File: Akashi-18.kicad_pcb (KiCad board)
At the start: 2 copper layers, 71.1 x 83.8 mm, 12 parts, among them Q1 DTC143Z, Q2 DTC143Z, Q3 DTC143Z, SW1 B3FS, SW2 B3FS, SW3 B3FS, U1 Pico

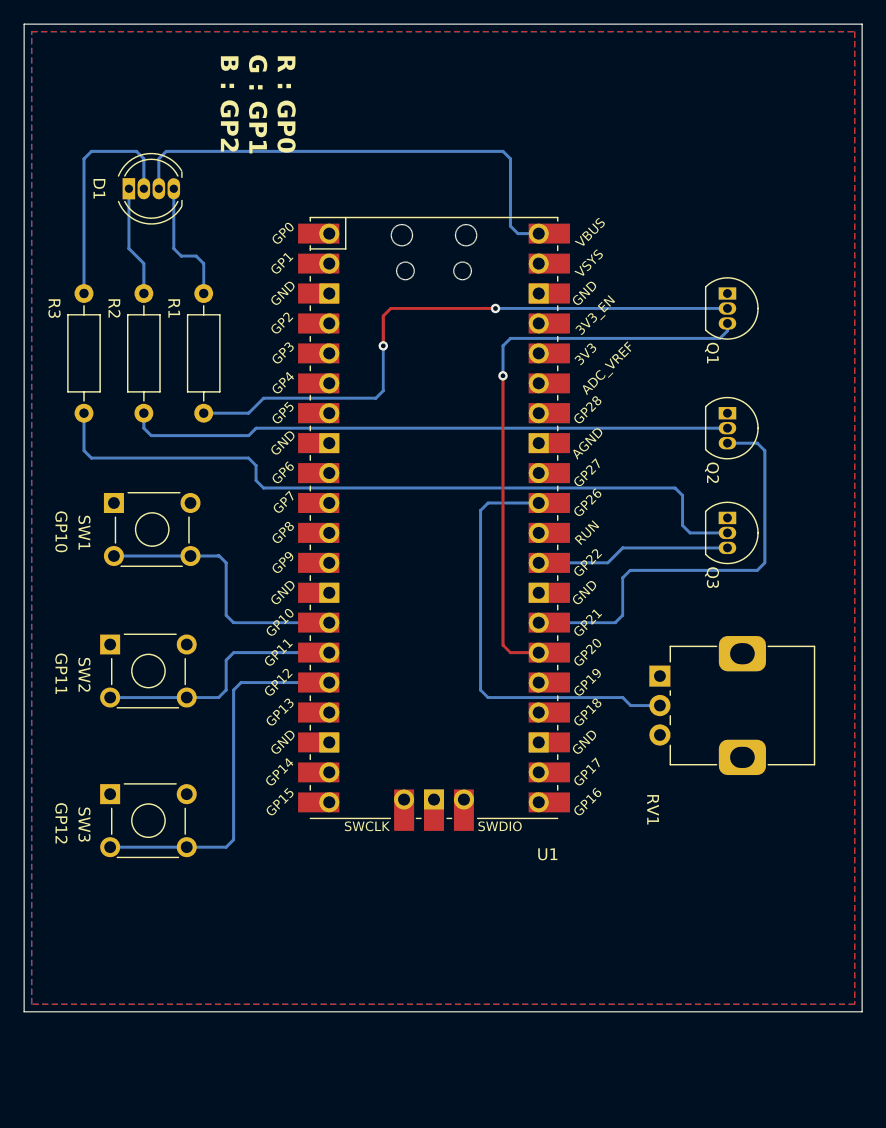
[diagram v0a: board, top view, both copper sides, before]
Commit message: All modified parts are registered to the local lib.
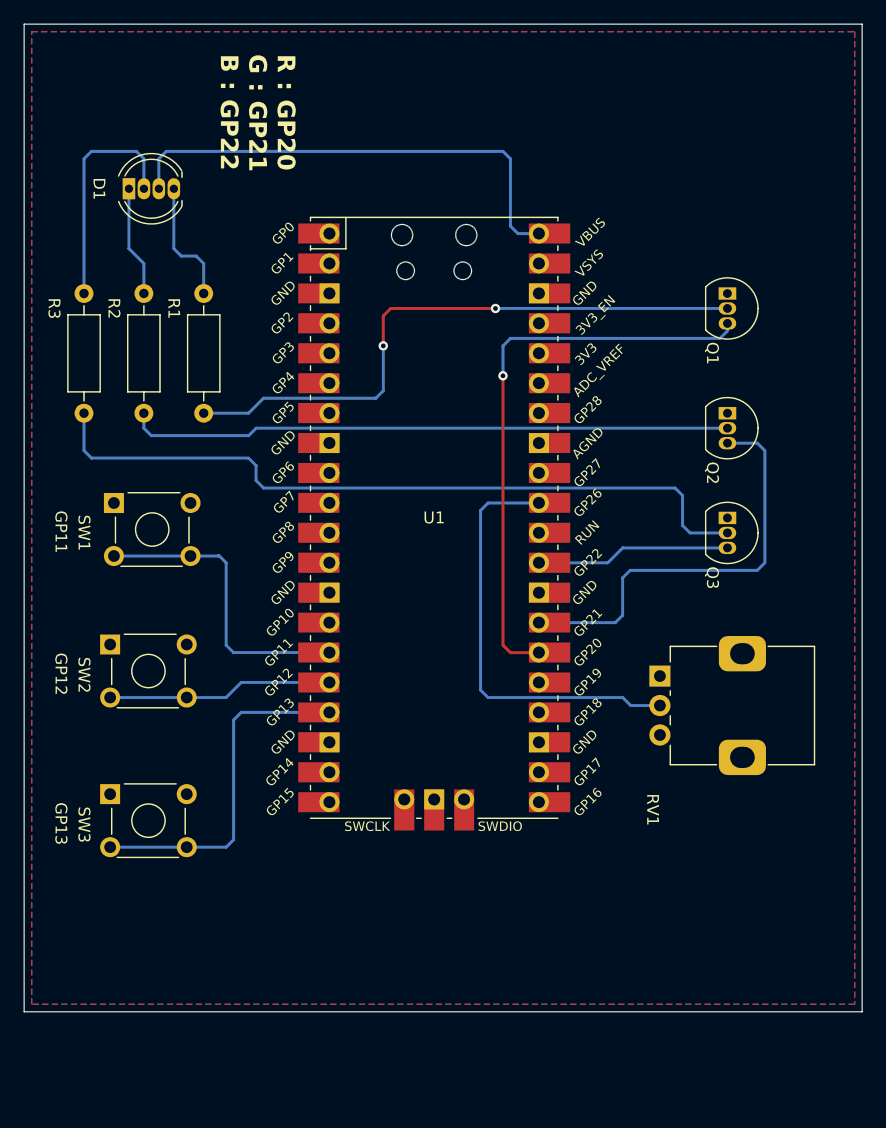
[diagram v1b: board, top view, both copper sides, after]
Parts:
- D1: footprint LED_THT:LED_D5.0mm-4_RGB -> My_Lib:LED_D5.0mm-4_RGB
- U1: footprint Rpi_Pico:RPi_Pico_SMD_TH -> My_Lib:RPi_Pico_SMD_TH
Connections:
- SW1 pad 2: Net-(U1-GPIO10) -> Net-(U1-GPIO11)
- SW2 pad 2: Net-(U1-GPIO11) -> Net-(U1-GPIO12)
- SW3 pad 2: Net-(U1-GPIO12) -> Net-(U1-GPIO13)
- U1 pad 14: Net-(U1-GPIO10) -> unconnected-(U1-GPIO10-Pad14)
- U1 pad 17: unconnected-(U1-GPIO13-Pad17) -> Net-(U1-GPIO13)
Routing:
- net Net-(U1-GPIO13): track 0.00 -> 29.3 mm
- net Net-(U1-GPIO10): track 23.3 -> 0.00 mm
- net Net-(U1-GPIO12): track 31.8 -> 19.1 mm
- net Net-(U1-GPIO11): track 21.7 -> 25.8 mm
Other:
- board text added: "GP13"
- board text added: "Pico Trainer"
- board text added: "R : GP20 G : GP21 B : GP22"
- board text removed: "GP10"
- board text removed: "R : GP0 G : GP1 B : GP2"

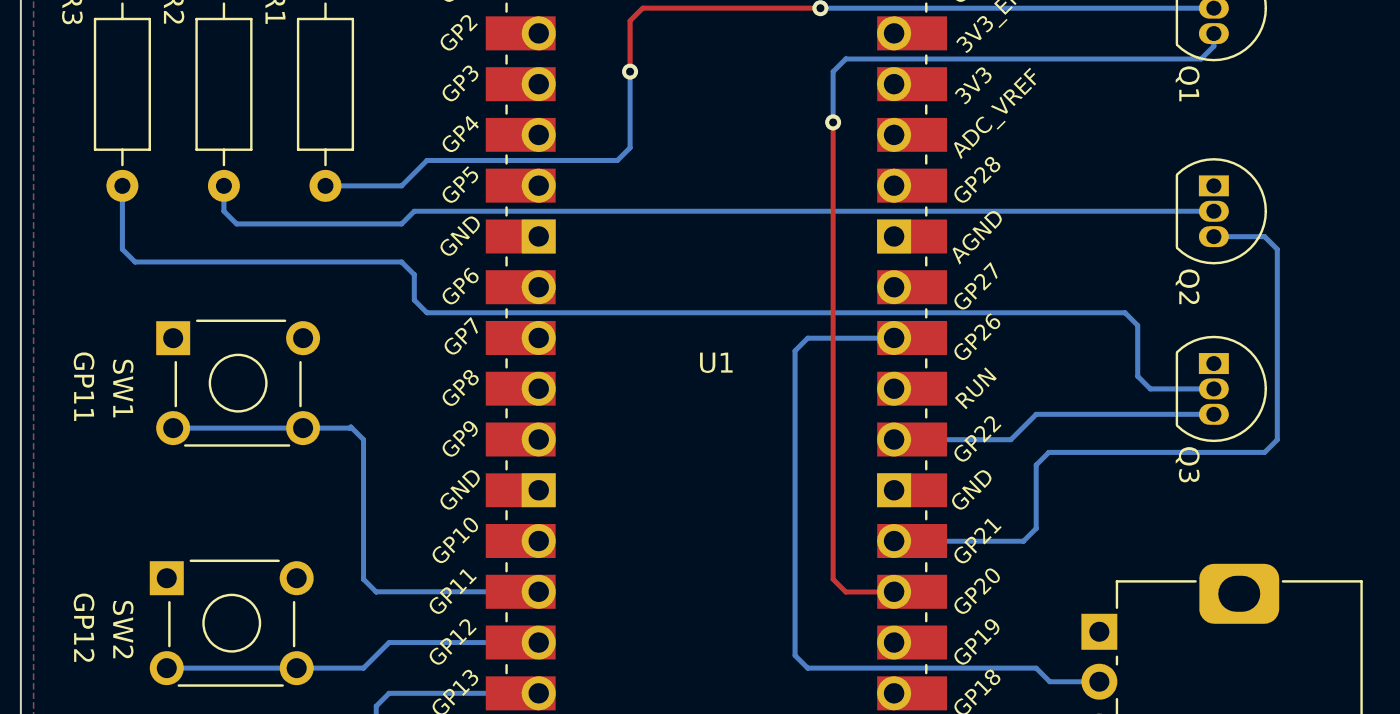
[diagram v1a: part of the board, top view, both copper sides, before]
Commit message: Adjust the space of transistor.
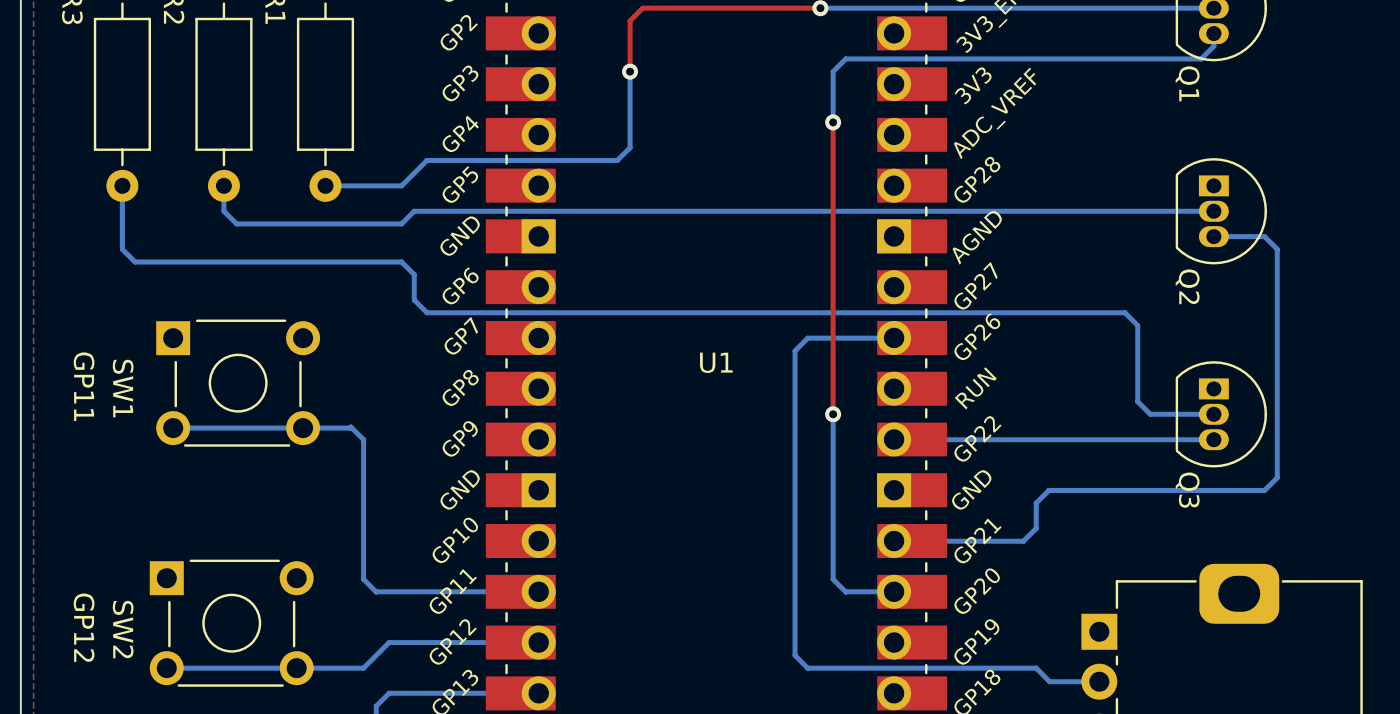
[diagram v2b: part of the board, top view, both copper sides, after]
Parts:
- R1: value R -> 220
- R2: value R -> 180
- R3: value R -> 91
- moved Q3 1.27 mm to (148.6, 94.0)
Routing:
- net Net-(Q3-C): track 62.9 -> 64.2 mm
- net /BLUE: track 16.5 -> 16.0 mm
- net /RED: vias 1 -> 2
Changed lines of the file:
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@@
         (effects (font (size 1 1) (thickness 0.15)))
     )
-    (fp_text value "R" (at 5.08 2.37 90) (layer "F.Fab")
+    (fp_text value "220" (at 5.08 2.37 90) (layer "F.Fab")
         (effects (font (size 1 1) (thickness 0.15)))
     )
@@
         (effects (font (size 1 1) (thickness 0.15)))
     )
-    (fp_text value "R" (at 5.08 2.37 90) (layer "F.Fab")
+    (fp_text value "91" (at 5.08 2.37 90) (layer "F.Fab")
         (effects (font (size 1 1) (thickness 0.15)))
     )
@@
         (effects (font (size 1 1) (thickness 0.15)))
     )
-    (fp_text value "R" (at 5.08 2.37 90) (layer "F.Fab")
+    (fp_text value "180" (at 5.08 2.37 90) (layer "F.Fab")
         (effects (font (size 1 1) (thickness 0.15)))
     )
@@
   )
   (footprint "Package_TO_SOT_THT:TO-92_Inline" (layer "F.Cu")
-    (at 148.59 92.71 -90)
+    (at 148.59 93.98 -90)
     (descr "TO-92 leads in-line, narrow, oval pads, drill 0.75mm (see NXP sot054_po.pdf)")
     (tags "to-92 sc-43 sc-43a sot54 PA33 transistor")
@@
   (segment (start 109.22 82.55) (end 107.95 83.82) (width 0.25) (layer "B.Cu") (net 6))
   (segment (start 119.38 81.915) (end 118.745 82.55) (width 0.25) (layer "B.Cu") (net 6))
-  (segment (start 129.54 103.505) (end 130.175 104.14) (width 0.25) (layer "F.Cu") (net 7))
-  (segment (start 129.54 80.645) (end 129.54 103.505) (width 0.25) (layer "F.Cu") (net 7))
-  (segment (start 130.175 104.14) (end 132.575 104.14) (width 0.25) (layer "F.Cu") (net 7))
+  (segment (start 129.54 80.645) (end 129.54 95.25) (width 0.25) (layer "F.Cu") (net 7))
+  (via (at 129.54 95.25) (size 0.8) (drill 0.4) (layers "F.Cu" "B.Cu") (net 7))
   (via (at 129.54 80.645) (size 0.8) (drill 0.4) (layers "F.Cu" "B.Cu") (net 7))
   (segment (start 147.955 77.47) (end 130.175 77.47) (width 0.25) (layer "B.Cu") (net 7))
+  (segment (start 130.175 104.14) (end 129.54 103.505) (width 0.25) (layer "B.Cu") (net 7))
+  (segment (start 129.54 103.505) (end 129.54 95.25) (width 0.25) (layer "B.Cu") (net 7))
   (segment (start 148.59 76.835) (end 147.955 77.47) (width 0.25) (layer "B.Cu") (net 7))
   (segment (start 129.54 78.105) (end 129.54 80.645) (width 0.25) (layer "B.Cu") (net 7))
+  (segment (start 132.59 104.13) (end 130.185 104.13) (width 0.25) (layer "B.Cu") (net 7))
+  (segment (start 130.185 104.13) (end 130.175 104.14) (width 0.25) (layer "B.Cu") (net 7))
   (segment (start 148.59 76.2) (end 148.59 76.835) (width 0.25) (layer "B.Cu") (net 7))
   (segment (start 130.175 77.47) (end 129.54 78.105) (width 0.25) (layer "B.Cu") (net 7))
@@
   (segment (start 99.695 85.725) (end 99.06 85.09) (width 0.25) (layer "B.Cu") (net 8))
   (segment (start 99.06 85.09) (end 99.06 83.82) (width 0.25) (layer "B.Cu") (net 8))
-  (segment (start 148.59 86.36) (end 151.13 86.36) (width 0.25) (layer "B.Cu") (net 9))
-  (segment (start 151.13 97.155) (end 140.335 97.155) (width 0.25) (layer "B.Cu") (net 9))
-  (segment (start 151.765 96.52) (end 151.13 97.155) (width 0.25) (layer "B.Cu") (net 9))
-  (segment (start 139.7 100.965) (end 139.065 101.6) (width 0.25) (layer "B.Cu") (net 9))
-  (segment (start 139.7 97.79) (end 139.7 100.965) (width 0.25) (layer "B.Cu") (net 9))
-  (segment (start 140.335 97.155) (end 139.7 97.79) (width 0.25) (layer "B.Cu") (net 9))
-  (segment (start 151.13 86.36) (end 151.765 86.995) (width 0.25) (layer "B.Cu") (net 9))
-  (segment (start 151.765 86.995) (end 151.765 96.52) (width 0.25) (layer "B.Cu") (net 9))
-  (segment (start 139.065 101.6) (end 132.575 101.6) (width 0.25) (layer "B.Cu") (net 9))
-  (segment (start 145.415 93.98) (end 144.78 93.345) (width 0.25) (layer "B.Cu") (net 10))
-  (segment (start 94.615 87.63) (end 93.98 86.995) (width 0.25) (layer "B.Cu") (net 10))
-  (segment (start 108.585 89.535) (end 108.585 88.265) (width 0.25) (layer "B.Cu") (net 10))
-  (segment (start 144.78 90.805) (end 144.145 90.17) (width 0.25) (layer "B.Cu") (net 10))
-  (segment (start 144.145 90.17) (end 109.22 90.17) (width 0.25) (layer "B.Cu") (net 10))
-  (segment (start 107.95 87.63) (end 94.615 87.63) (width 0.25) (layer "B.Cu") (net 10))
-  (segment (start 148.59 93.98) (end 145.415 93.98) (width 0.25) (layer "B.Cu") (net 10))
-  (segment (start 108.585 88.265) (end 107.95 87.63) (width 0.25) (layer "B.Cu") (net 10))
-  (segment (start 93.98 86.995) (end 93.98 83.82) (width 0.25) (layer "B.Cu") (net 10))
-  (segment (start 144.78 93.345) (end 144.78 90.805) (width 0.25) (layer "B.Cu") (net 10))
-  (segment (start 109.22 90.17) (end 108.585 89.535) (width 0.25) (layer "B.Cu") (net 10))
-  (segment (start 139.7 95.25) (end 138.43 96.52) (width 0.25) (layer "B.Cu") (net 11))
-  (segment (start 138.43 96.52) (end 132.575 96.52) (width 0.25) (layer "B.Cu") (net 11))
-  (segment (start 148.59 95.25) (end 139.7 95.25) (width 0.25) (layer "B.Cu") (net 11))
+  (segment (start 139.065 101.6) (end 139.7 100.965) (width 0.25) (layer "B.Cu") (net 9))
+  (segment (start 139.7 99.695) (end 140.335 99.06) (width 0.25) (layer "B.Cu") (net 9))
+  (segment (start 151.765 98.425) (end 151.765 86.995) (width 0.25) (layer "B.Cu") (net 9))
+  (segment (start 151.13 99.06) (end 151.765 98.425) (width 0.25) (layer "B.Cu") (net 9))
+  (segment (start 151.13 86.36) (end 148.59 86.36) (width 0.25) (layer "B.Cu") (net 9))
+  (segment (start 140.335 99.06) (end 151.13 99.06) (width 0.25) (layer "B.Cu") (net 9))
+  (segment (start 139.7 100.965) (end 139.7 99.695) (width 0.25) (layer "B.Cu") (net 9))
+  (segment (start 151.765 86.995) (end 151.13 86.36) (width 0.25) (layer "B.Cu") (net 9))
+  (segment (start 132.575 101.6) (end 139.065 101.6) (width 0.25) (layer "B.Cu") (net 9))
+  (segment (start 108.585 89.535) (end 109.22 90.17) (width 0.25) (layer "B.Cu") (net 10))
+  (segment (start 107.95 87.63) (end 108.585 88.265) (width 0.25) (layer "B.Cu") (net 10))
+  (segment (start 144.145 90.17) (end 144.78 90.805) (width 0.25) (layer "B.Cu") (net 10))
+  (segment (start 108.585 88.265) (end 108.585 89.535) (width 0.25) (layer "B.Cu") (net 10))
+  (segment (start 93.98 83.82) (end 93.98 86.995) (width 0.25) (layer "B.Cu") (net 10))
+  (segment (start 145.415 95.25) (end 148.59 95.25) (width 0.25) (layer "B.Cu") (net 10))
+  (segment (start 144.78 90.805) (end 144.78 94.615) (width 0.25) (layer "B.Cu") (net 10))
+  (segment (start 144.78 94.615) (end 145.415 95.25) (width 0.25) (layer "B.Cu") (net 10))
+  (segment (start 93.98 86.995) (end 94.615 87.63) (width 0.25) (layer "B.Cu") (net 10))
+  (segment (start 109.22 90.17) (end 144.145 90.17) (width 0.25) (layer "B.Cu") (net 10))
+  (segment (start 94.615 87.63) (end 107.95 87.63) (width 0.25) (layer "B.Cu") (net 10))
+  (segment (start 132.575 96.52) (end 148.59 96.52) (width 0.25) (layer "B.Cu") (net 11))
   (segment (start 140.38 108.63) (end 139.7 107.95) (width 0.25) (layer "B.Cu") (net 12))
   (segment (start 128.27 91.44) (end 132.575 91.44) (width 0.25) (layer "B.Cu") (net 12))
